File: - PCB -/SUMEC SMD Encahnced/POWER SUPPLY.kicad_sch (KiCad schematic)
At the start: 7 parts, among them U7 LM1084IS-5.0/NOPB, U8 LM1084IS-3.3/NOPB

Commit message: QRE Array - WIP
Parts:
- C11, C13: value 10uF.stabl -> 10uF.stabl.tantal
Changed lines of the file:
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@@
       (effects (font (size 1.27 1.27)) (justify left))
     )
-    (property "Value" "10uF.stabl" (at 139.7 55.88 0)
+    (property "Value" "10uF.stabl.tantal" (at 139.7 55.88 0)
       (effects (font (size 1.27 1.27)) (justify left))
     )
@@
       (effects (font (size 1.27 1.27)) (justify left))
     )
-    (property "Value" "10uF.stabl" (at 209.55 55.88 0)
+    (property "Value" "10uF.stabl.tantal" (at 209.55 55.88 0)
       (effects (font (size 1.27 1.27)) (justify left))
     )

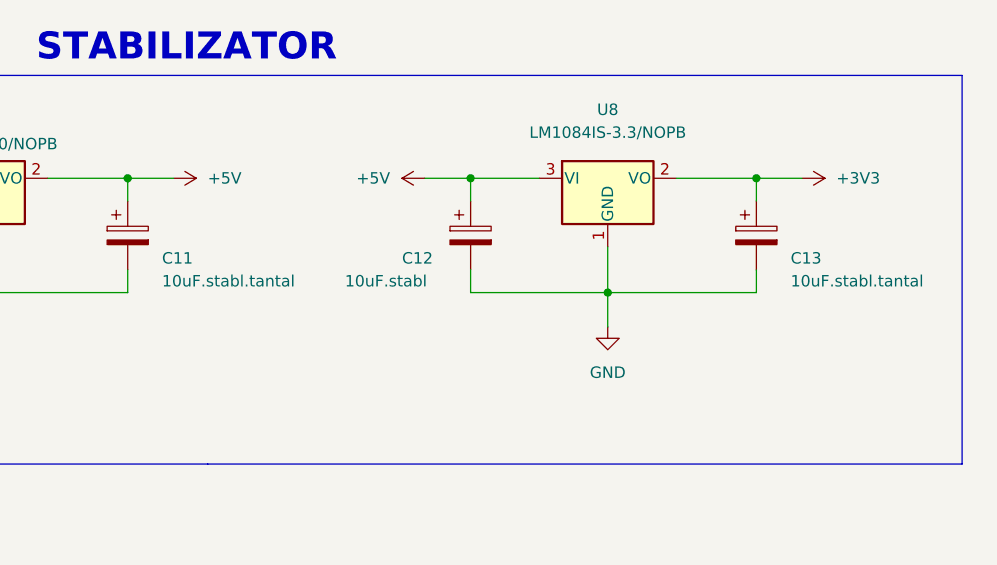
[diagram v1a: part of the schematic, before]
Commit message: Revert "Merge branch 'sumec-main' of https://github.com/menmenson/RoboCop into sumec-main"
This reverts commit dbf205ac3b02d72b1b38e86a27b286e1b118f9d4, reversing
changes made to f2387d167bca73d6a0741a06b82f65a42dfb555a.
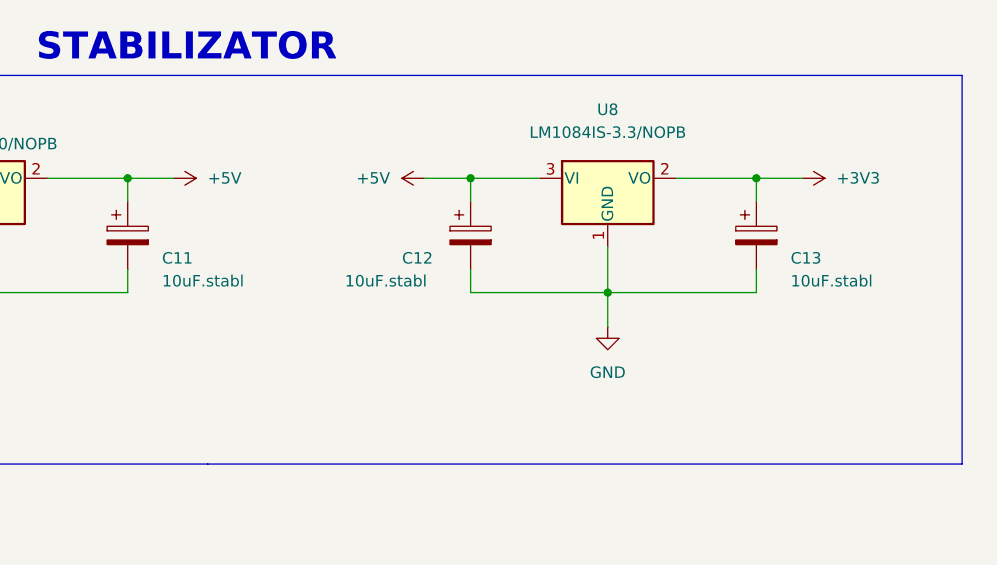
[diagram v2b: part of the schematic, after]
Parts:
- C11, C13: value 10uF.stabl.tantal -> 10uF.stabl
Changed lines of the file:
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@@
       (effects (font (size 1.27 1.27)) (justify left))
     )
-    (property "Value" "10uF.stabl.tantal" (at 139.7 55.88 0)
+    (property "Value" "10uF.stabl" (at 139.7 55.88 0)
       (effects (font (size 1.27 1.27)) (justify left))
     )
@@
       (effects (font (size 1.27 1.27)) (justify left))
     )
-    (property "Value" "10uF.stabl.tantal" (at 209.55 55.88 0)
+    (property "Value" "10uF.stabl" (at 209.55 55.88 0)
       (effects (font (size 1.27 1.27)) (justify left))
     )
